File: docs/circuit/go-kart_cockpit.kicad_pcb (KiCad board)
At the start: 2 copper layers, 96.8 x 66.2 mm, 37 parts, among them P1 Power, Q1 IRL3803, X1 Start/Stop/Rückwärts, X10 CS, X11 J3, X12 PB6, X13 AVR-ISP-10, X14 24V Hupe, X2 Taster rechts (male), X3 Taster links (male)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

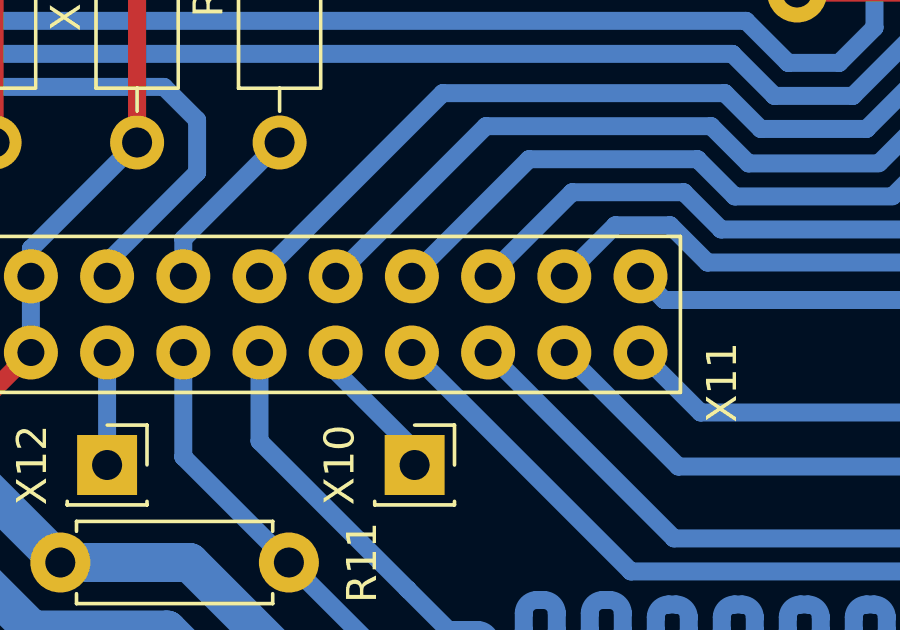
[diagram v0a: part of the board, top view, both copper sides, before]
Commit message: fix(PCB): ISP is actually connected to UART0 instead of SPI
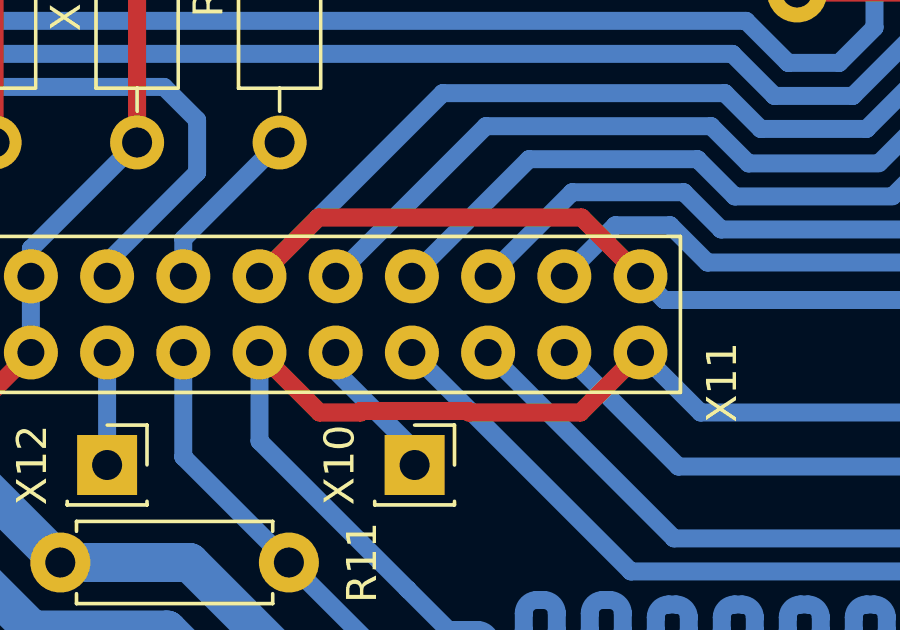
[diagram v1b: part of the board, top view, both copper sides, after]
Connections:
- X11 pad 15: PB3_MISO -> PE1_TXD0_PB3_MISO
- X11 pad 16: PB2_MOSI -> PE0_RXD0_PB2_MOSI
- X11 pad 25: PE1_TXD0 -> PE1_TXD0_PB3_MISO
- X11 pad 26: PE0_RXD0 -> PE0_RXD0_PB2_MOSI
- X13 pad 1: PB2_MOSI -> PE0_RXD0_PB2_MOSI
- X13 pad 9: PB3_MISO -> PE1_TXD0_PB3_MISO
- X9 pad 2: PE0_RXD0 -> PE0_RXD0_PB2_MOSI
- X9 pad 6: PE1_TXD0 -> PE1_TXD0_PB3_MISO
- XB10 pad 1: PE1_TXD0 -> PE1_TXD0_PB3_MISO
- XB10 pad 2: PE1_TXD0 -> PE1_TXD0_PB3_MISO
- XB11 pad 1: PB3_MISO -> PE1_TXD0_PB3_MISO
- XB11 pad 2: PB3_MISO -> PE1_TXD0_PB3_MISO
- XB9 pad 1: PE0_RXD0 -> PE0_RXD0_PB2_MOSI
- XB9 pad 2: PE0_RXD0 -> PE0_RXD0_PB2_MOSI
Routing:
- net PE1_TXD0_PB3_MISO: track 0.00 -> 208.5 mm
- net PE0_RXD0_PB2_MOSI: track 0.00 -> 183.5 mm
- net PB3_MISO: track 143.0 -> 0.00 mm
- net PB2_MOSI: track 110.5 -> 0.00 mm
- net PE0_RXD0: track 58.5 -> 0.00 mm
- net PE1_TXD0: track 51.2 -> 0.00 mm
